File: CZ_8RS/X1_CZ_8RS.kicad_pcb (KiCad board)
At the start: 2 copper layers, 137 x 140 mm, 68 parts, among them IC1 74LS541, IC10 74LS04, IC11 74LS20, IC12 8251, IC13 74LS08, IC14 74LS01, IC15 MAX232, IC16 74LS74, IC17 74LS32, IC18 MAX232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

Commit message: Add files via upload
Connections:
- IC16 pad 5: (no net) -> Net-(IC16-Pad5)
- IC16 pad 6: Net-(IC16-Pad6) -> (no net)
- IC17 pad 4: Net-(IC16-Pad6) -> Net-(IC16-Pad5)
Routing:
- net Net-(IC16-Pad5): track 0.00 -> 40.7 mm, vias 0 -> 1
- net Net-(IC16-Pad6): track 36.2 -> 0.00 mm
- net Net-(IC20-Pad1): track 78.1 -> 81.3 mm
- net ~RESET: track 171.0 -> 169.2 mm
- net Net-(IC18-Pad8): track 39.6 -> 41.1 mm
- net ~IACK: track 148.9 -> 147.6 mm
- net RESET: track 217.6 -> 216.7 mm
- net IRQ_RX: track 176.6 -> 175.7 mm
- net IRQ_TX: track 64.1 -> 63.2 mm
- net ~CS: track 102.6 -> 101.8 mm
- net Net-(IC11-Pad9): track 12.2 -> 11.4 mm
- net Net-(IC12-Pad6): track 91.2 -> 90.6 mm
- net RXRDY: track 159.4 -> 158.8 mm
- net AB10: track 82.5 -> 82.0 mm
- net ~IEO: track 75.8 -> 75.3 mm
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
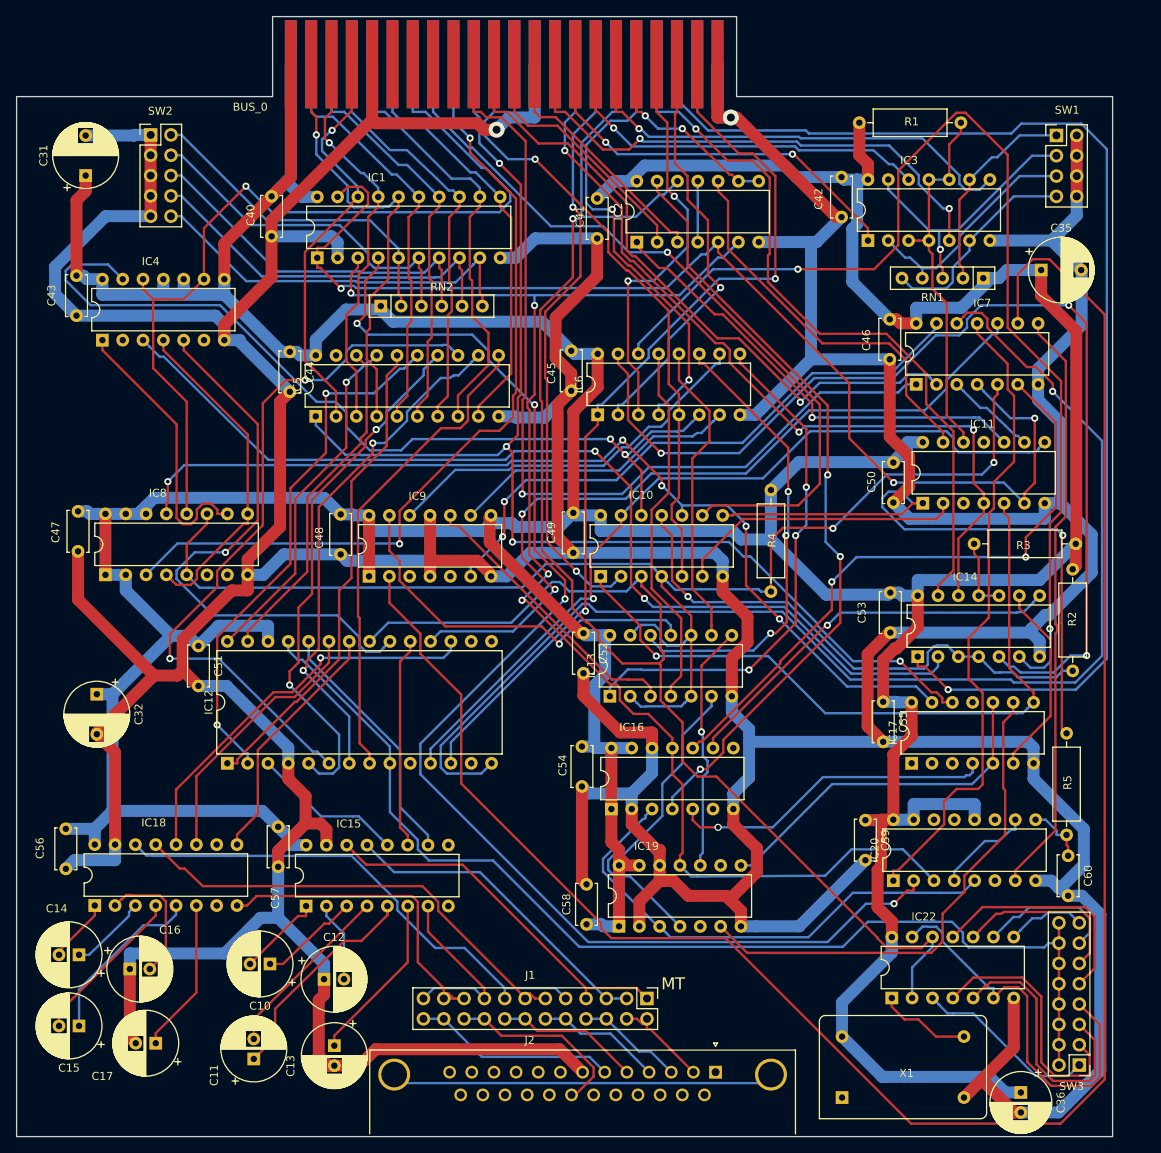
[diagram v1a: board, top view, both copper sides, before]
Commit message: corrected siosel, siord, and siowr line tag names
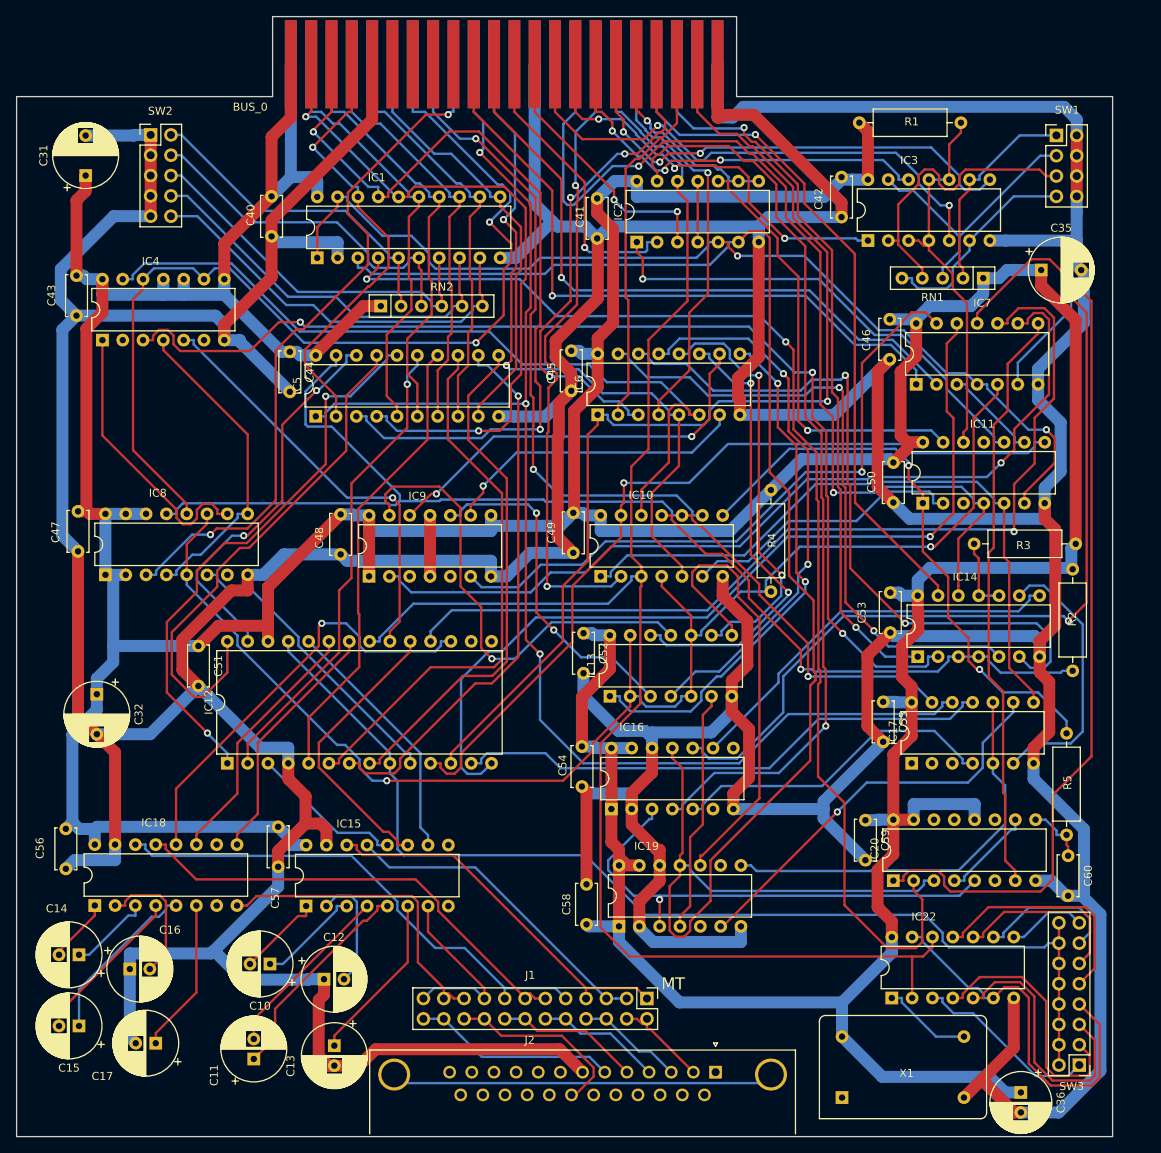
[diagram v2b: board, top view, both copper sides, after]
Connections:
- IC12 pad 10: (no net) -> ~SIOWR
- IC12 pad 13: (no net) -> ~SIORD
- IC17 pad 11: (no net) -> ~SIORD
- IC5 pad 19: (no net) -> ~SIOSEL
- IC8 pad 6: (no net) -> ~SIOWR
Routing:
- net Net-(IC7-Pad9): track 246.5 -> 109.8 mm, vias 0 -> 1
- net ~SIORD: track 0.00 -> 68.0 mm
- net ~EXWAIT: track 153.1 -> 93.0 mm, vias 1 -> 2
- net GND: track 1031.5 -> 1087.3 mm, vias 2 -> 0
- net DB1: track 49.5 -> 103.7 mm, vias 1 -> 2
- net ~CS0: track 131.2 -> 79.8 mm, vias 3 -> 2
- net ~CS1: track 138.5 -> 89.7 mm
- net RXRDY: track 158.8 -> 110.5 mm
- net IRQ_RX: track 175.7 -> 212.8 mm, vias 4 -> 0
- net ~SIOWR: track 0.00 -> 36.8 mm
- net Net-(IC20-Pad1): track 81.3 -> 117.9 mm
- net Net-(IC16-Pad10): track 78.8 -> 114.0 mm
- net DB2: track 55.8 -> 86.1 mm, vias 1 -> 2
- net AB11: track 113.2 -> 84.1 mm
- net Net-(IC13-Pad8): track 31.0 -> 57.0 mm, vias 1 -> 0
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
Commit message: added component names and jumper values
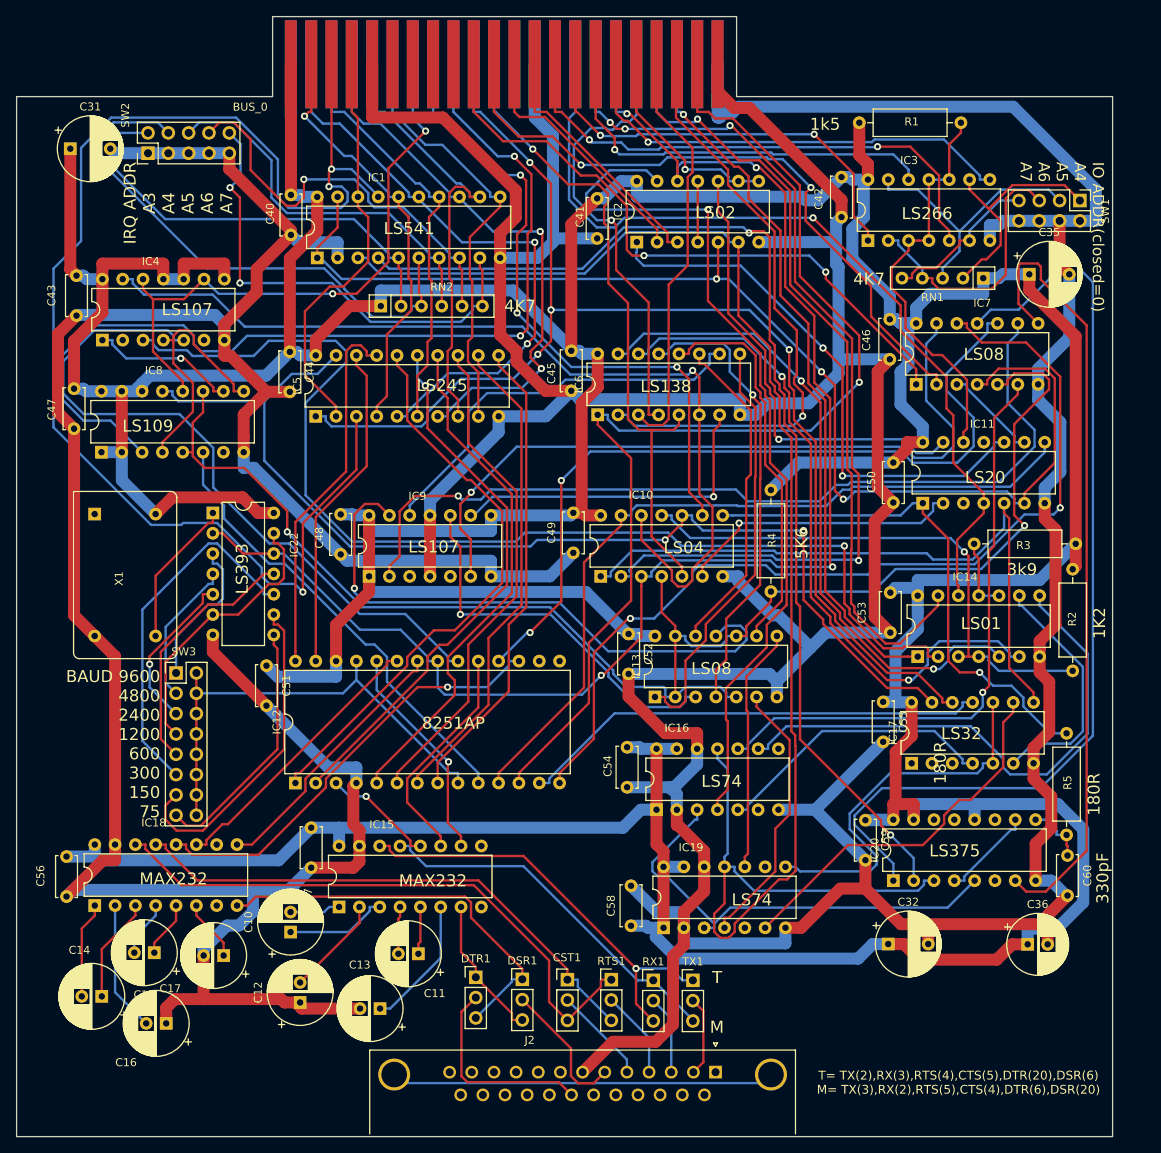
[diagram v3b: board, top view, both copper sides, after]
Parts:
- removed J1: CONN_02x12, Connector_PinHeader_2.54mm:PinHeader_2x12_P2.54mm_Vertical
- added CST1: Conn_01x03, Connector_PinHeader_2.54mm:PinHeader_1x03_P2.54mm_Vertical, F.Cu at (196.9, 213.4)
- added DSR1: Conn_01x03, Connector_PinHeader_2.54mm:PinHeader_1x03_P2.54mm_Vertical, F.Cu at (191.2, 213.4)
- added DTR1: Conn_01x03, Connector_PinHeader_2.54mm:PinHeader_1x03_P2.54mm_Vertical, F.Cu at (185.4, 213.1)
- added RTS1: Conn_01x03, Connector_PinHeader_2.54mm:PinHeader_1x03_P2.54mm_Vertical, F.Cu at (202.4, 213.4)
- added RX1: Conn_01x03, Connector_PinHeader_2.54mm:PinHeader_1x03_P2.54mm_Vertical, F.Cu at (207.6, 213.5)
- added TX1: Conn_01x03, Connector_PinHeader_2.54mm:PinHeader_1x03_P2.54mm_Vertical, F.Cu at (212.6, 213.5)
- moved SW3 123.1 mm to (148.0, 175.1), turned to 0 degrees
- moved X1 118.5 mm to (137.8, 155.2), turned to 270 degrees
- moved IC22 104.3 mm to (152.6, 155.1), turned to 0 degrees
- moved C32 103.7 mm to (237.0, 209.0), turned to 0 degrees
- moved C11 24.4 mm to (178.2, 210.2), turned to 180 degrees
- moved C36 18.5 mm to (254.4, 209.0), turned to 0 degrees
- moved C47 15.3 mm to (135.2, 139.5)
- moved IC8 15.3 mm to (138.6, 147.5)
- moved C17 13.9 mm to (153.9, 210.4)
- moved C15 13.1 mm to (145.2, 210.0)
- moved C51 8.86 mm to (159.3, 174.2)
- moved IC12 8.86 mm to (162.9, 188.8)
- moved SW1 8.65 mm to (260.9, 116.0), turned to 270 degrees
- moved C16 8.18 mm to (146.7, 218.9), turned to 180 degrees
- moved C13 7.36 mm to (173.5, 217.0), turned to 180 degrees
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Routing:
- net TxRxCLK: track 138.0 -> 59.6 mm
- net +5V: track 757.7 -> 825.6 mm
- net GND: track 1087.3 -> 1019.6 mm
- net DB1: track 103.7 -> 170.8 mm, vias 2 -> 3
- net CLK: track 124.9 -> 76.2 mm
- net Net-(IC16-Pad10): track 114.0 -> 75.2 mm, vias 2 -> 1
- net ~IEO: track 79.0 -> 116.7 mm, vias 2 -> 4
- net SIOCLK: track 53.4 -> 87.9 mm, vias 1 -> 0
- net DB2: track 86.1 -> 53.1 mm, vias 2 -> 1
- net ~WE: track 88.4 -> 120.0 mm
- net AB1: track 47.6 -> 75.4 mm, vias 0 -> 1
- net ~IACK: track 125.1 -> 151.8 mm, vias 2 -> 3
- net Net-(IC13-Pad8): track 57.0 -> 30.7 mm
- net Net-(IC20-Pad7): track 73.6 -> 98.3 mm
- net Net-(IC1-Pad6): track 44.4 -> 68.8 mm
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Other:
- board text added: "180R"
- board text added: "1K2"
- board text added: "1k5"
- board text added: "330pF"
- board text added: "3k9"
- board text added: "4K7"
- board text added: "5K6"
- board text added: "8251AP"
- board text added: "BAUD 9600 4800 2400 1200 600 300 150 75"
- board text added: "IO ADDR(closed=0) A4 A5 A6 A7"
- board text added: "IRQ ADDR A3 A4 A5 A6 A7"
- board text added: "LS01"
- board text added: "LS02"
- board text added: "LS04"
- board text added: "LS08"
- board text added: "LS107"
- board text added: "LS109"
- board text added: "LS138"
- board text added: "LS20"
- board text added: "LS245"
- board text added: "LS266"
- board text added: "LS32"
- board text added: "LS375"
- board text added: "LS393"
- board text added: "LS541"
- board text added: "LS74"
- board text added: "MAX232"
- board text added: "T= TX(2),RX(3),RTS(4),CTS(5),DTR(20),DSR(6) M= TX(3),RX(2),RTS(5),CTS(4),DTR(6),DSR(20)"
